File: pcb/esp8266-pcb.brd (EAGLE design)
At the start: 45.7 x 45.7 mm, 20 parts

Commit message: Notofication LED replaced with 1206 package.
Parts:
- LED1: device adafruit:LED3MM -> led:1206
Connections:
- net N$1: now also LED1.C; no longer LED1.K
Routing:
- net +3V3: track 76.0 -> 76.5 mm
- net N$1: track 4.13 -> 4.19 mm, vias 0 -> 1
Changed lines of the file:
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@@
 <attribute name="VALUE" x="14.478" y="0.508" size="0.4064" layer="27"/>
 </element>
-<element name="LED1" library="adafruit" package="LED3MM" value="RED" x="22.86" y="40.64" smashed="yes">
-<attribute name="NAME" x="20.701" y="36.957" size="1.27" layer="25" font="vector" ratio="15"/>
+<element name="LED1" library="led" package="1206" value="RED" x="22.86" y="40.64" smashed="yes">
+<attribute name="NAME" x="20.701" y="37.973" size="1.27" layer="25" font="vector" ratio="15"/>
 <attribute name="VALUE" x="24.765" y="38.989" size="1.27" layer="27" ratio="10"/>
 </element>
@@
 </signal>
 <signal name="N$1">
-<contactref element="LED1" pad="K"/>
+<contactref element="LED1" pad="C"/>
 <contactref element="R1" pad="1"/>
-<wire x1="24.13" y1="40.64" x2="24.13" y2="36.51" width="0.4064" layer="16"/>
+<wire x1="24.282" y1="40.64" x2="24.282" y2="38.76" width="0.4064" layer="1"/>
+<wire x1="24.282" y1="38.76" x2="24.13" y2="38.608" width="0.4064" layer="1"/>
+<via x="24.13" y="38.608" extent="1-16" drill="0.6"/>
+<wire x1="24.13" y1="38.608" x2="24.13" y2="36.51" width="0.4064" layer="16"/>
 </signal>
 <signal name="VIN">
@@
 <wire x1="26.543" y1="27.813" x2="23.114" y2="31.242" width="0.6096" layer="16"/>
 <wire x1="23.114" y1="31.242" x2="21.082" y2="33.274" width="0.6096" layer="1"/>
-<wire x1="21.082" y1="33.274" x2="21.082" y2="40.132" width="0.6096" layer="1"/>
-<wire x1="21.082" y1="40.132" x2="21.59" y2="40.64" width="0.6096" layer="1"/>
+<wire x1="21.082" y1="40.132" x2="21.438" y2="40.64" width="0.6096" layer="1"/>
 <contactref element="PWR" pad="2"/>
 <wire x1="26.543" y1="27.813" x2="32.131" y2="27.813" width="0.6096" layer="16"/>
@@
 <contactref element="R5" pad="2"/>
 <wire x1="39.37" y1="25.974" x2="37.338" y2="25.974" width="0.6096" layer="16"/>
+<wire x1="21.082" y1="33.274" x2="21.082" y2="40.284" width="0.4064" layer="1"/>
+<wire x1="21.082" y1="40.284" x2="21.438" y2="40.64" width="0.4064" layer="1"/>
 </signal>
 <signal name="N$3">

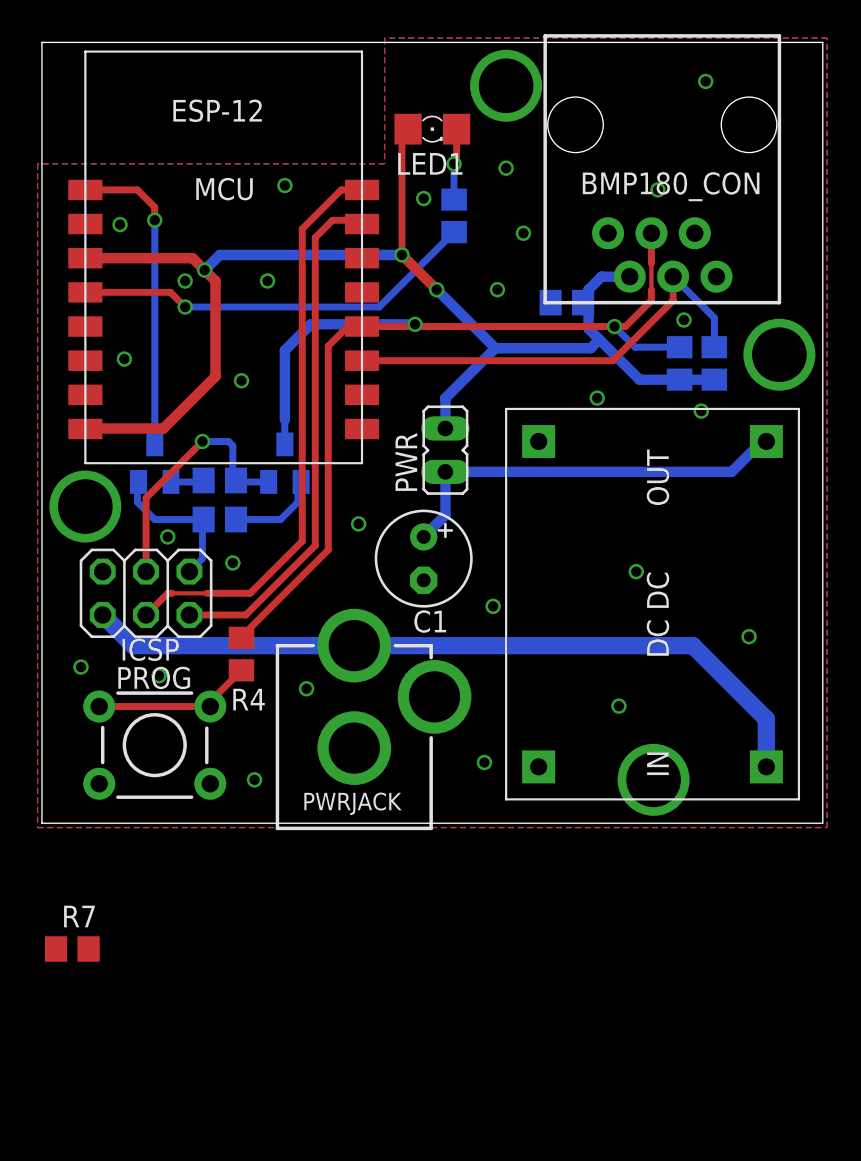
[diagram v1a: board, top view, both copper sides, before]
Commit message: Component rerouting.
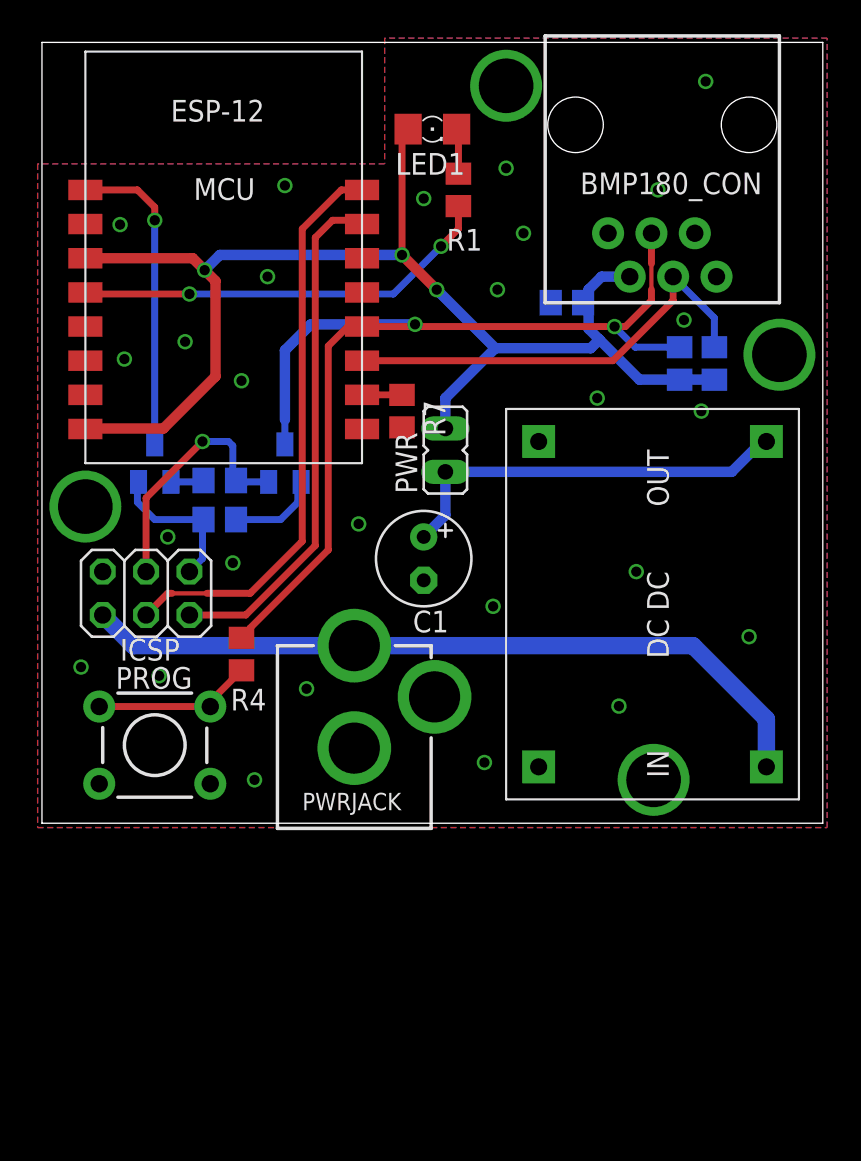
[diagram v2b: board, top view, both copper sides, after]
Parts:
- moved R7 36.9 mm to (21.1, 24.1), turned to 270 degrees
- moved R1 1.55 mm to (24.4, 37.1), flipped to the top
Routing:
- net N$5: track 0.00 -> 2.34 mm
- net N$1: track 4.19 -> 2.71 mm, vias 1 -> 0
- net GPIO16: track 23.8 -> 24.8 mm, vias 1 -> 2
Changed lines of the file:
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@@
 <attribute name="NAME" x="12.478" y="37.766" size="1.27" layer="21" font="vector" ratio="15" rot="R180"/>
 </element>
-<element name="R1" library="rcl" package="R0805" value="??R" x="24.13" y="35.56" smashed="yes" rot="MR270">
-<attribute name="NAME" x="22.733" y="33.274" size="1.27" layer="26" font="vector" ratio="15" rot="MR180"/>
-<attribute name="VALUE" x="23.749" y="33.02" size="1.27" layer="28" rot="MR180"/>
+<element name="R1" library="rcl" package="R0805" value="??R" x="24.384" y="37.084" smashed="yes" rot="R270">
+<attribute name="NAME" x="25.781" y="34.798" size="1.27" layer="25" font="vector" ratio="15" rot="R180"/>
+<attribute name="VALUE" x="24.765" y="34.544" size="1.27" layer="27" rot="R180"/>
 </element>
 <element name="T1" library="transistor" package="SOT23-BEC" value="" x="14.224" y="21.082" smashed="yes" rot="MR0">
@@
 </element>
 <element name="GOLD_ORB_SM1" library="NBitWonder" package="OSHW0" value="OSHWLOGO_GOLD_ORB_LG" x="24.638" y="19.05" rot="MR0"/>
-<element name="R7" library="rcl" package="R0805" value="12K" x="1.778" y="-7.366"/>
+<element name="R7" library="rcl" package="R0805" value="12K" x="21.082" y="24.13" rot="R270"/>
 </elements>
 <signals>
@@
 <via x="35.814" y="2.54" extent="1-16" drill="3.2"/>
 <via x="2.54" y="18.542" extent="1-16" drill="3.2"/>
-<via x="13.208" y="31.75" extent="1-16" drill="0.6"/>
+<via x="13.208" y="32.004" extent="1-16" drill="0.6"/>
 <via x="4.572" y="35.052" extent="1-16" drill="0.6"/>
 <via x="14.224" y="37.338" extent="1-16" drill="0.6"/>
@@
 <via x="12.446" y="2.54" extent="1-16" drill="0.6"/>
 <via x="38.862" y="43.434" extent="1-16" drill="0.6"/>
-<via x="8.382" y="31.75" extent="1-16" drill="0.6"/>
+<via x="8.382" y="28.194" extent="1-16" drill="0.6"/>
 <contactref element="R7" pad="2"/>
-<wire x1="3.3528" y1="2.3114" x2="2.728" y2="-7.366" width="0" layer="19" extent="1-1"/>
 </signal>
 <signal name="N$1">
 <contactref element="LED1" pad="C"/>
 <contactref element="R1" pad="1"/>
-<wire x1="24.282" y1="40.64" x2="24.282" y2="38.76" width="0.4064" layer="1"/>
-<wire x1="24.282" y1="38.76" x2="24.13" y2="38.608" width="0.4064" layer="1"/>
-<via x="24.13" y="38.608" extent="1-16" drill="0.6"/>
-<wire x1="24.13" y1="38.608" x2="24.13" y2="36.51" width="0.4064" layer="16"/>
+<wire x1="24.282" y1="40.64" x2="24.384" y2="40.64" width="0.4064" layer="1"/>
+<wire x1="24.384" y1="40.64" x2="24.384" y2="38.034" width="0.4064" layer="1"/>
 </signal>
 <signal name="VIN">
@@
 <contactref element="R1" pad="2"/>
 <contactref element="MCU" pad="12"/>
-<wire x1="2.54" y1="31.082" x2="7.526" y2="31.082" width="0.4064" layer="1"/>
-<wire x1="7.526" y1="31.082" x2="8.382" y2="30.226" width="0.4064" layer="1"/>
-<via x="8.382" y="30.226" extent="1-16" drill="0.6"/>
-<wire x1="8.382" y1="30.226" x2="19.746" y2="30.226" width="0.4064" layer="16"/>
-<wire x1="19.746" y1="30.226" x2="24.13" y2="34.61" width="0.4064" layer="16"/>
+<wire x1="24.384" y1="36.134" x2="24.384" y2="34.798" width="0.4064" layer="1"/>
+<wire x1="24.384" y1="34.798" x2="23.368" y2="33.782" width="0.4064" layer="1"/>
+<via x="23.368" y="33.782" extent="1-16" drill="0.6"/>
+<wire x1="23.368" y1="33.782" x2="20.574" y2="30.988" width="0.4064" layer="16"/>
+<wire x1="20.574" y1="30.988" x2="8.636" y2="30.988" width="0.4064" layer="16"/>
+<via x="8.636" y="30.988" extent="1-16" drill="0.6"/>
+<wire x1="8.636" y1="30.988" x2="2.634" y2="30.988" width="0.4064" layer="1"/>
+<wire x1="2.634" y1="30.988" x2="2.54" y2="31.082" width="0.4064" layer="1"/>
 </signal>
 <signal name="N$2">
@@
 <contactref element="MCU" pad="2"/>
 <contactref element="R7" pad="1"/>
-<wire x1="0.828" y1="-7.366" x2="18.74" y2="25.082" width="0" layer="19" extent="1-1"/>
+<wire x1="18.74" y1="25.082" x2="21.082" y2="25.082" width="0.4064" layer="1"/>
+<wire x1="21.082" y1="25.082" x2="21.082" y2="25.08" width="0.4064" layer="1"/>
 </signal>
 </signals>

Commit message: Updated schematics.
Changed sensor connection pins.
Changed pin order on ICSP header.
Added RX and TX ping to unused RJ-11 pins.
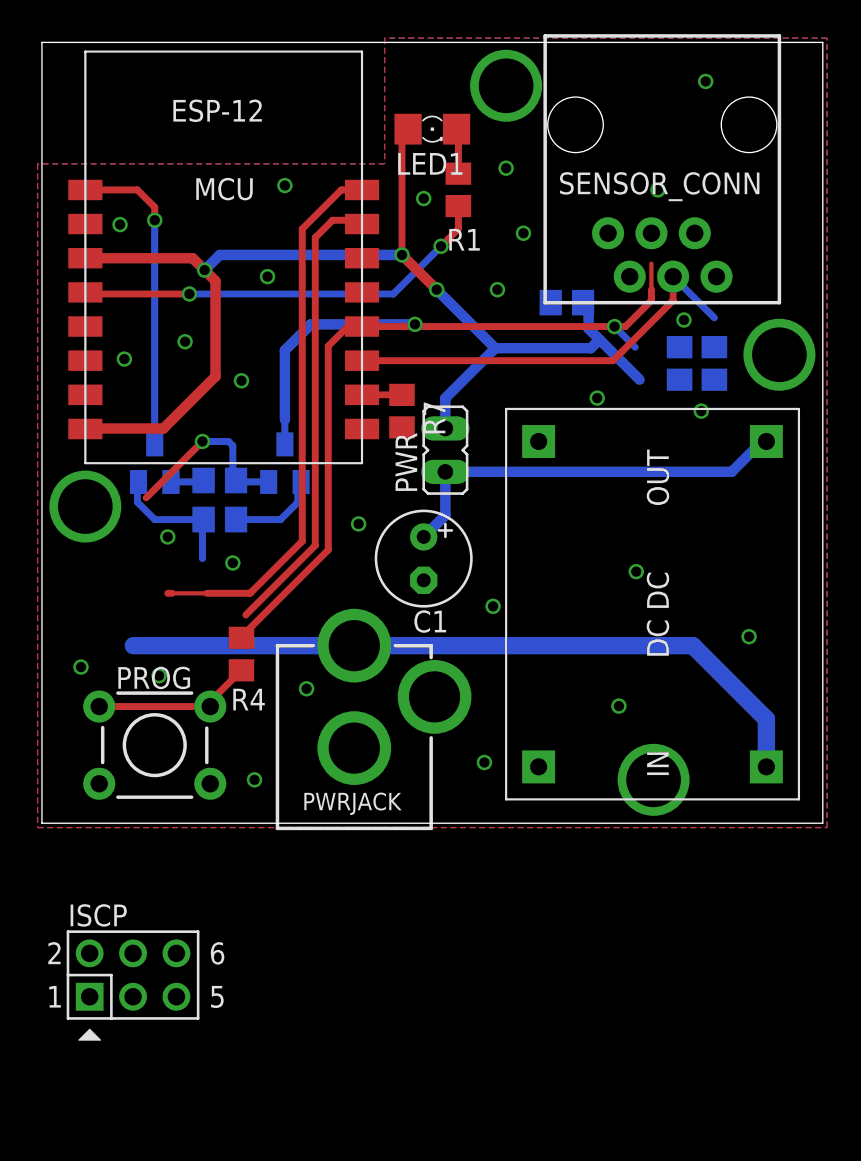
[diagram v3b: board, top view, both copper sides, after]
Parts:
- removed ICSP: (no value), pinhead:2X03
- added ISCP: CON_HEADER_PRG_AVR_ICSP-PTH, dp_devices:HEADER_PRG_2X03
- renumbered BMP180_CON to SENSOR_CONN
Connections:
- new net GPIO14: MCU.13, R6.1, SENSOR_CONN.4
- net +3V3: now also C2.2, ISCP.2; no longer C2.1
- net DTR: now also ISCP.3; no longer ICSP.4
- net GND: now also C2.1, ISCP.6; no longer C2.2, ICSP.2
- net GPIO0: no longer R6.1, SENSOR_CONN.4
- net RST: now also ISCP.5; no longer ICSP.6
- net RXD: now also ISCP.1, SENSOR_CONN.1; no longer ICSP.5
- net TXD: now also ISCP.4, SENSOR_CONN.6; no longer ICSP.3
- net VIN: no longer ICSP.1
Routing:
- net +3V3: track 76.5 -> 68.1 mm
- net GPIO0: track 61.4 -> 57.0 mm
- net DTR: track 15.0 -> 10.7 mm
- net RXD: track 30.5 -> 27.2 mm
- net VIN: track 44.2 -> 41.6 mm
- net TXD: track 33.7 -> 31.9 mm
- net GPIO2: track 26.2 -> 24.5 mm
- net RST: track 8.90 -> 7.82 mm

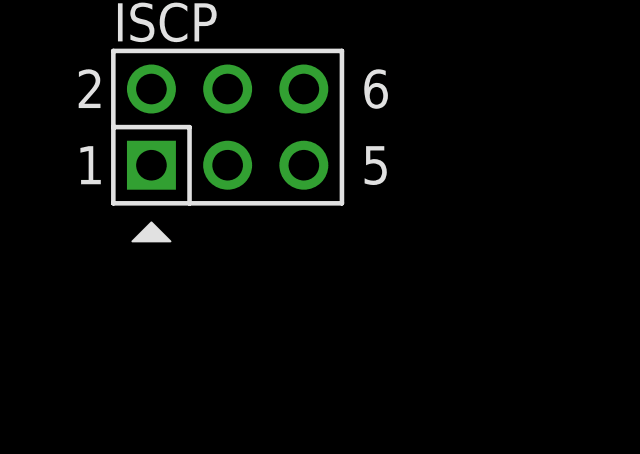
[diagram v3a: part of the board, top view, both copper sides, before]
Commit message: Added jumper to ICSP voltage pin.
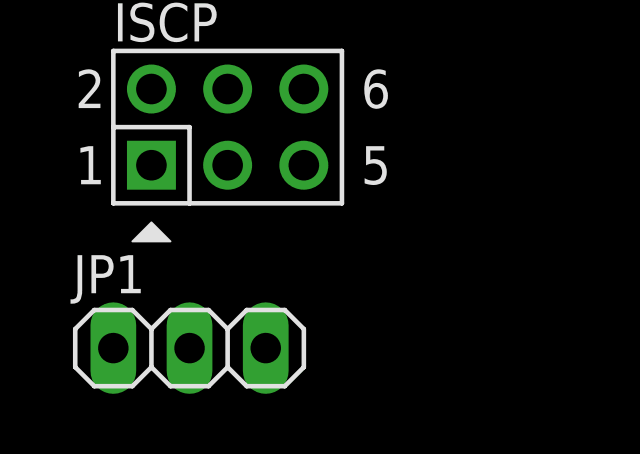
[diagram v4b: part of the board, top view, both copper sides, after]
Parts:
- added JP1: (no value), pinhead:1X03
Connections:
- new net N$6: ISCP.2, JP1.2
- net +3V3: now also JP1.1; no longer ISCP.2
- net VIN: now also JP1.3
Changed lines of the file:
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@@
 <element name="R7" library="rcl" package="R0805" value="12K" x="21.082" y="24.13" rot="R270"/>
 <element name="ISCP" library="dp_devices" package="HEADER_PRG_2X03" value="CON_HEADER_PRG_AVR_ICSP-PTH" x="5.334" y="-8.89"/>
+<element name="JP1" library="pinhead" package="1X03" value="" x="4.064" y="-16.256"/>
 </elements>
 <signals>
@@
 <wire x1="38.116" y1="10.398" x2="42.418" y2="6.096" width="1.016" layer="16"/>
 <wire x1="42.418" y1="6.096" x2="42.418" y2="3.302" width="1.016" layer="16"/>
+<contactref element="JP1" pad="3"/>
+<wire x1="6.604" y1="-16.256" x2="5.35" y2="10.398" width="0" layer="19" extent="16-16"/>
 </signal>
 <signal name="+3V3">
@@
 <wire x1="21.082" y1="33.274" x2="21.082" y2="40.284" width="0.4064" layer="1"/>
 <wire x1="21.082" y1="40.284" x2="21.438" y2="40.64" width="0.4064" layer="1"/>
-<contactref element="ISCP" pad="2"/>
 <contactref element="SENSOR_CONN" pad="5"/>
 <contactref element="R5" pad="2"/>
 <contactref element="R6" pad="2"/>
 <contactref element="C2" pad="2"/>
+<contactref element="JP1" pad="1"/>
 <wire x1="32.004" y1="30.16" x2="34.417" y2="32.004" width="0" layer="19" extent="16-16"/>
 <wire x1="29.784" y1="30.48" x2="32.004" y2="30.16" width="0" layer="19" extent="16-16"/>
 <wire x1="37.338" y1="25.974" x2="34.986" y2="25.974" width="0" layer="19" extent="16-16"/>
 <wire x1="39.37" y1="25.974" x2="37.338" y2="25.974" width="0" layer="19" extent="16-16"/>
-<wire x1="2.794" y1="-7.62" x2="2.54" y2="23.082" width="0" layer="19" extent="1-1"/>
+<wire x1="1.524" y1="-16.256" x2="2.54" y2="23.082" width="0" layer="19" extent="1-1"/>
 </signal>
 <signal name="N$3">
@@
 <wire x1="2.54" y1="29.082" x2="35.687" y2="34.544" width="0" layer="19" extent="1-1"/>
 </signal>
+<signal name="N$6">
+<contactref element="ISCP" pad="2"/>
+<contactref element="JP1" pad="2"/>
+<wire x1="2.794" y1="-7.62" x2="4.064" y2="-16.256" width="0" layer="19" extent="1-1"/>
+</signal>
 </signals>

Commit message: Board routing.
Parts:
- removed JP1: (no value), pinhead:1X03
- added ICSPPWR: (no value), pinhead:1X03
- moved ISCP 21.1 mm to (5.59, 12.2), turned to 180 degrees
- moved C1 1.27 mm to (23.6, 15.5)
- moved C2 0.36 mm to (31.0, 30.7), turned to 90 degrees
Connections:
- net +3V3: now also ICSPPWR.1; no longer JP1.1
- net N$6: now also ICSPPWR.2; no longer JP1.2
- net VIN: now also ICSPPWR.3; no longer JP1.3
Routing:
- net GPIO14: track 0.00 -> 42.6 mm, vias 0 -> 3
- net RXD: track 27.2 -> 60.1 mm, vias 0 -> 2
- net GPIO0: track 57.0 -> 29.9 mm, vias 2 -> 1
- net TXD: track 31.9 -> 51.4 mm, vias 0 -> 2
- net +3V3: track 68.1 -> 85.8 mm
- net N$6: track 0.00 -> 13.1 mm
- net VIN: track 41.6 -> 32.7 mm
- net RST: track 7.82 -> 13.7 mm
- net DTR: track 10.7 -> 16.5 mm
- net GPIO2: track 24.5 -> 26.2 mm
- net N$2: track 23.9 -> 23.3 mm

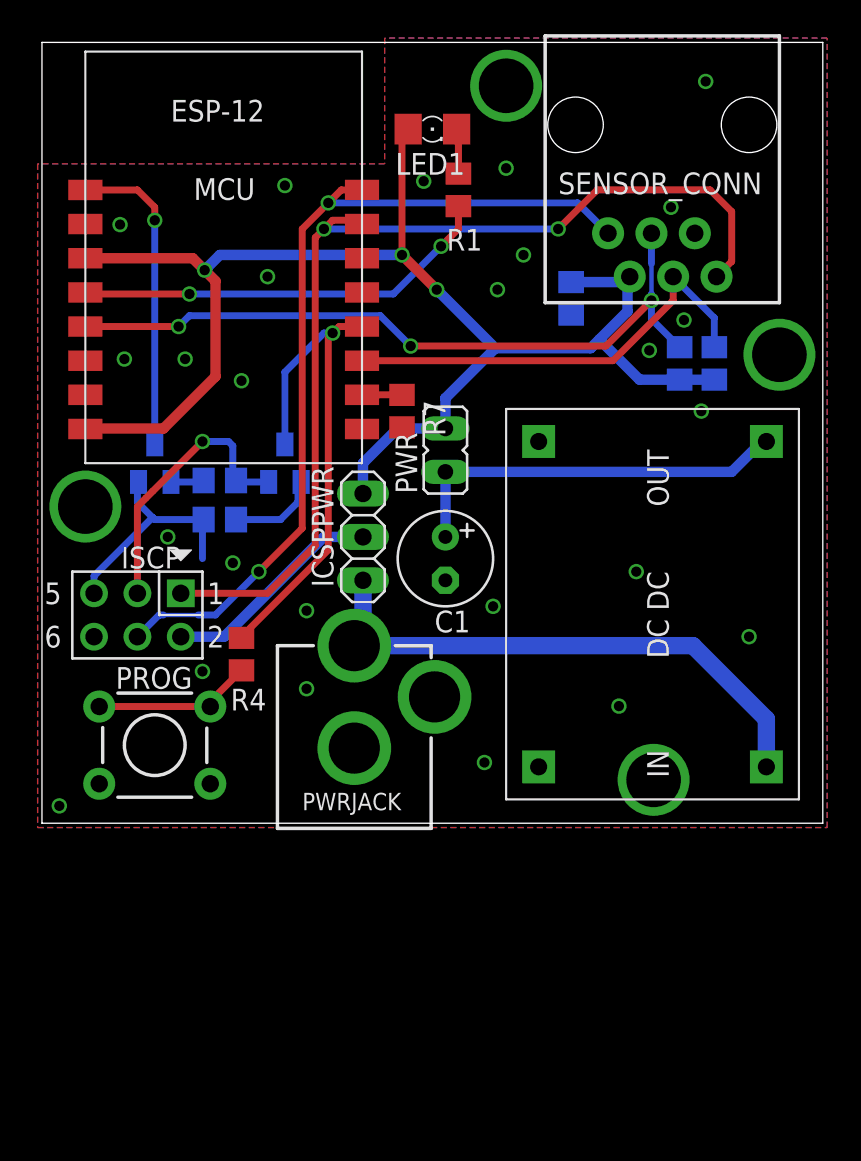
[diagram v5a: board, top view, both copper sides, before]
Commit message: Updated ISP header.
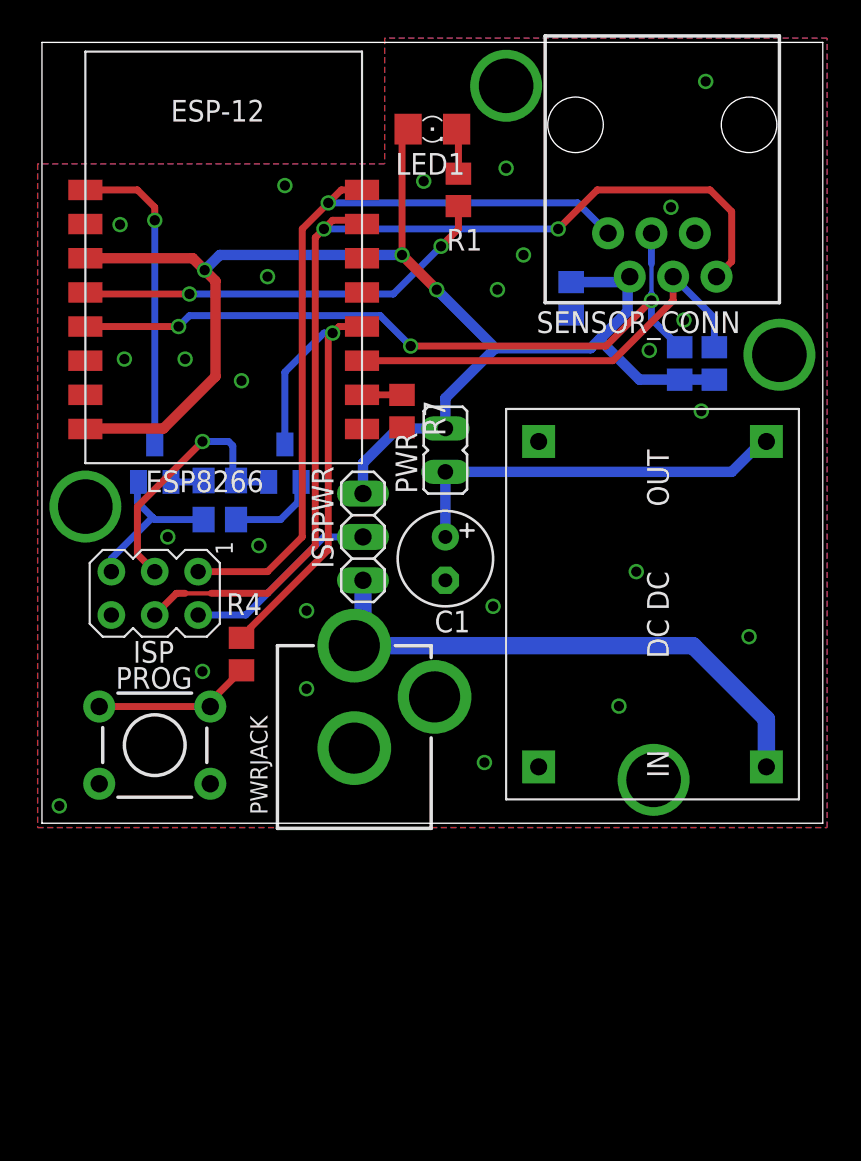
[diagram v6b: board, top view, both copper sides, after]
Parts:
- removed ISCP: CON_HEADER_PRG_AVR_ICSP-PTH, dp_devices:HEADER_PRG_2X03
- added ISP: AVRISP-6, adafruit:AVRISP
- renumbered ICSPPWR to ISPPWR, MCU to ESP8266
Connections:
- net DTR: now also ISP.3; no longer ISCP.3
- net GND: now also ISP.6; no longer ISCP.6
- net N$6: now also ISP.2; no longer ISCP.2
- net RST: now also ISP.5; no longer ISCP.5
- net RXD: now also ISP.4; no longer ISCP.1
- net TXD: now also ISP.1; no longer ISCP.4
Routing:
- net TXD: track 51.4 -> 46.5 mm, vias 2 -> 1
- net RST: track 13.7 -> 9.78 mm
- net RXD: track 60.1 -> 62.1 mm
- net N$6: track 13.1 -> 11.5 mm
- net DTR: track 16.5 -> 15.6 mm
